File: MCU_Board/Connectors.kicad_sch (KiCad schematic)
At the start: 1 part, among them J2 USB_B_Micro

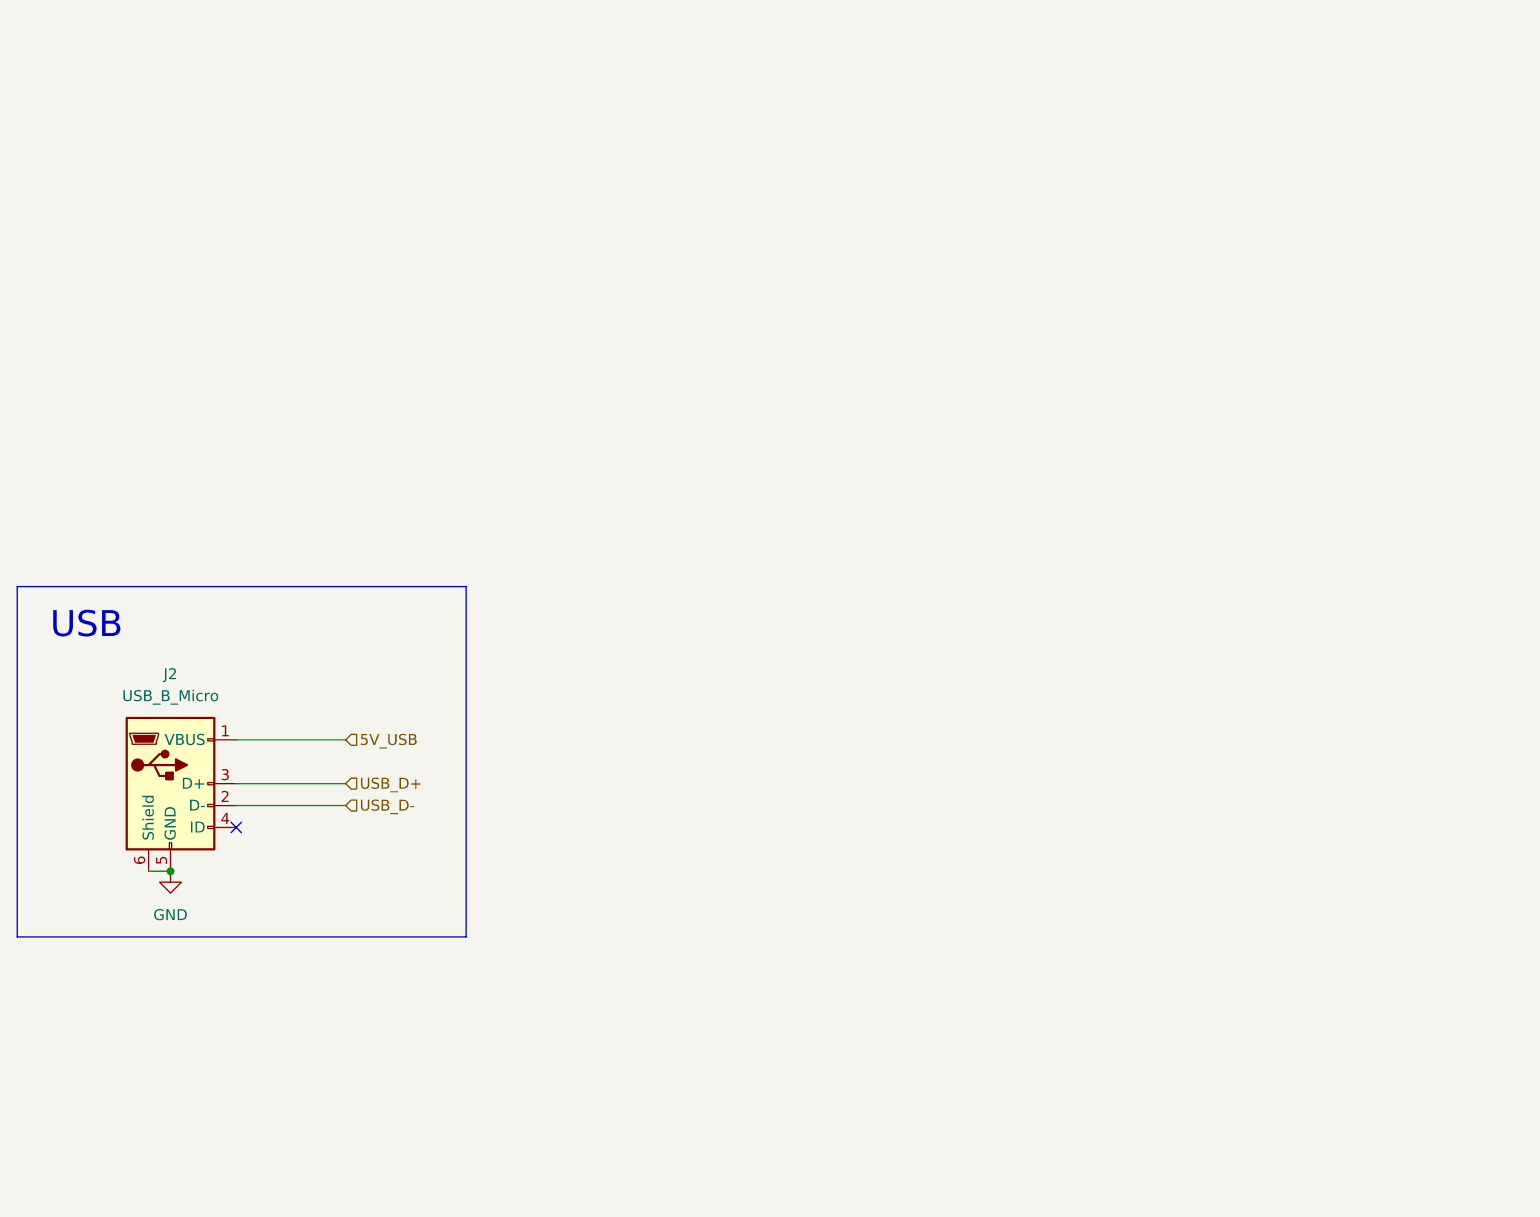
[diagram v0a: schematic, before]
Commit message: Added JTAG connector to MCU board
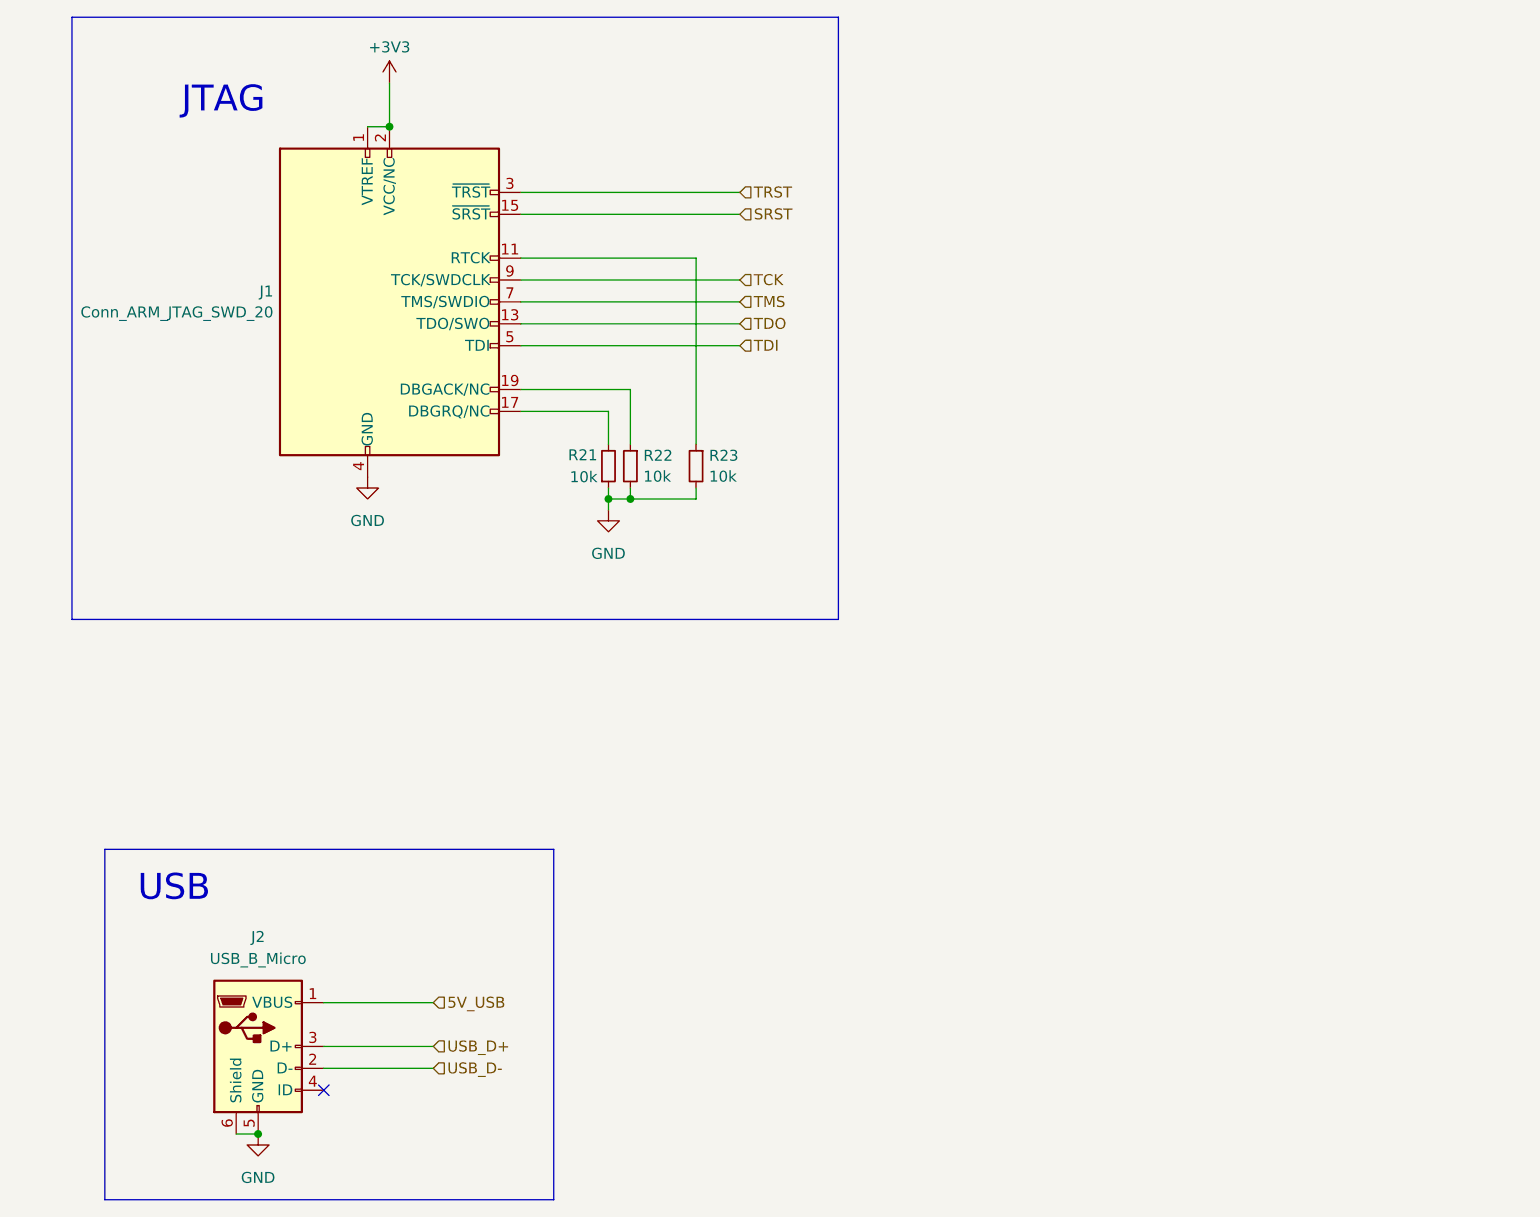
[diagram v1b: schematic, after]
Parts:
- added J1: Conn_ARM_JTAG_SWD_20, Connector_PinHeader_1.27mm:PinHeader_2x10_P1.27mm_Vertical_SMD, symbol Connector:Conn_ARM_JTAG_SWD_20
- added R21, R22, R23: 10k, symbol Device:R_Small
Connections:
- net GND: now also J1.10 (GND), J1.12 (GND), J1.14 (GND), J1.16 (GND), J1.18 (GND), J1.20 (GND), J1.4 (GND), J1.6 (GND), J1.8 (GND), R21.1, R22.2, R23.2
- new net: J1.19 (DBGACK/NC), R22.1
- new net: J1.11 (RTCK), R23.1
- new net: J1.17 (DBGRQ/NC), R21.2
- new net +3V3: J1.1 (VTREF), J1.2 (VCC/NC)
- new net SRST: J1.15 (~{SRST})
- new net TCK: J1.9 (TCK/SWDCLK)
- new net TDI: J1.5 (TDI)
- new net TDO: J1.13 (TDO/SWO)
- new net TMS: J1.7 (TMS/SWDIO)
- new net TRST: J1.3 (~{TRST})
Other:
- note added: "JTAG"
- moved on the sheet: J2

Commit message: Added a header for the VCO controls
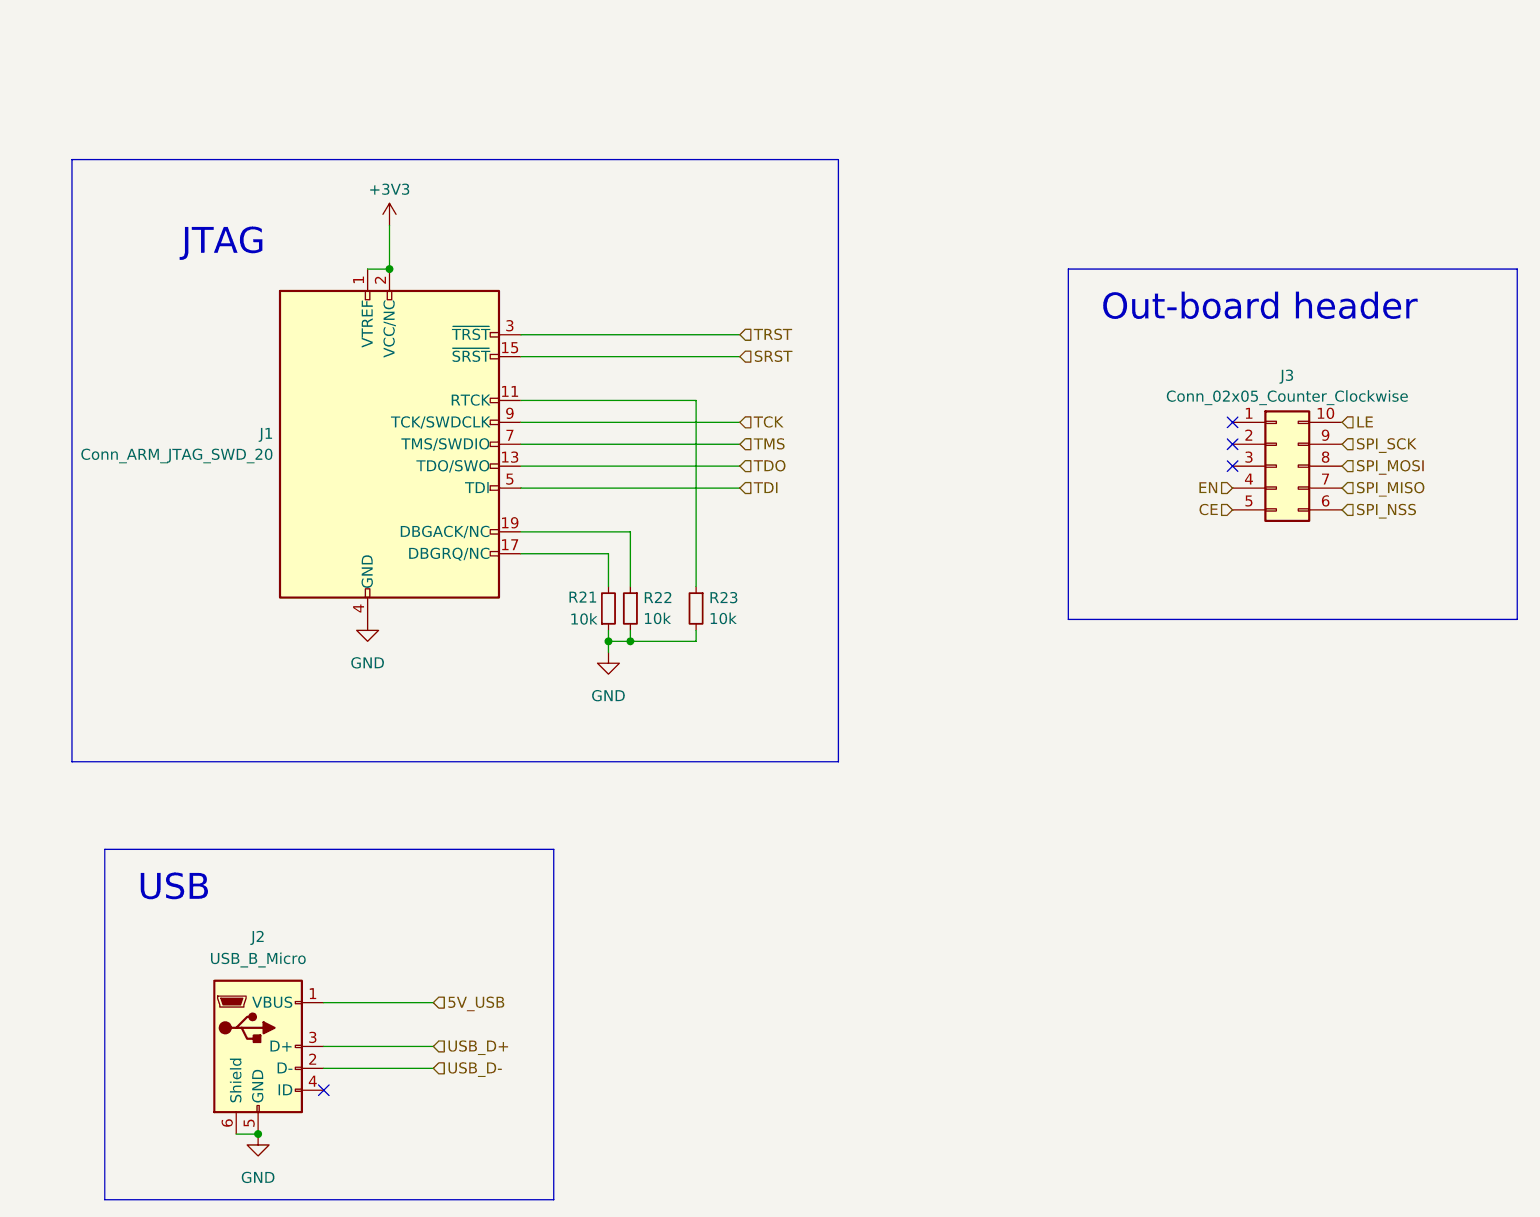
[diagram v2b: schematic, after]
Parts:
- added J3: Conn_02x05_Counter_Clockwise, Connector_PinHeader_2.54mm:PinHeader_2x05_P2.54mm_Vertical, symbol Connector_Generic:Conn_02x05_Counter_Clockwise
- R21, R22, R23: footprint (none) -> Resistor_SMD:R_0603_1608Metric_Pad0.98x0.95mm_HandSolder
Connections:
- new net CE: J3.5 (Pin_5)
- new net EN: J3.4 (Pin_4)
- new net LE: J3.10 (Pin_10)
- new net SPI_MISO: J3.7 (Pin_7)
- new net SPI_MOSI: J3.8 (Pin_8)
- new net SPI_NSS: J3.6 (Pin_6)
- new net SPI_SCK: J3.9 (Pin_9)
- no-connect marks 1 -> 4
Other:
- note added: "Out-board header"
- moved on the sheet: J1, R21, R22, R23
